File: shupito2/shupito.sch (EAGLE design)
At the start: 89 parts, among them IC2 74LVC1T45, IC3 74LVC1T45, IC4 74LVC1T45, IC5 74LVC1T45, IC6 ATXMEGA32A4U-AU, IC7 TPS73033DBV, Q1 BC807W-1907646, Q10 1758094, Q11 PDTC123YU-1757992, Q2 NX2301P-1894738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

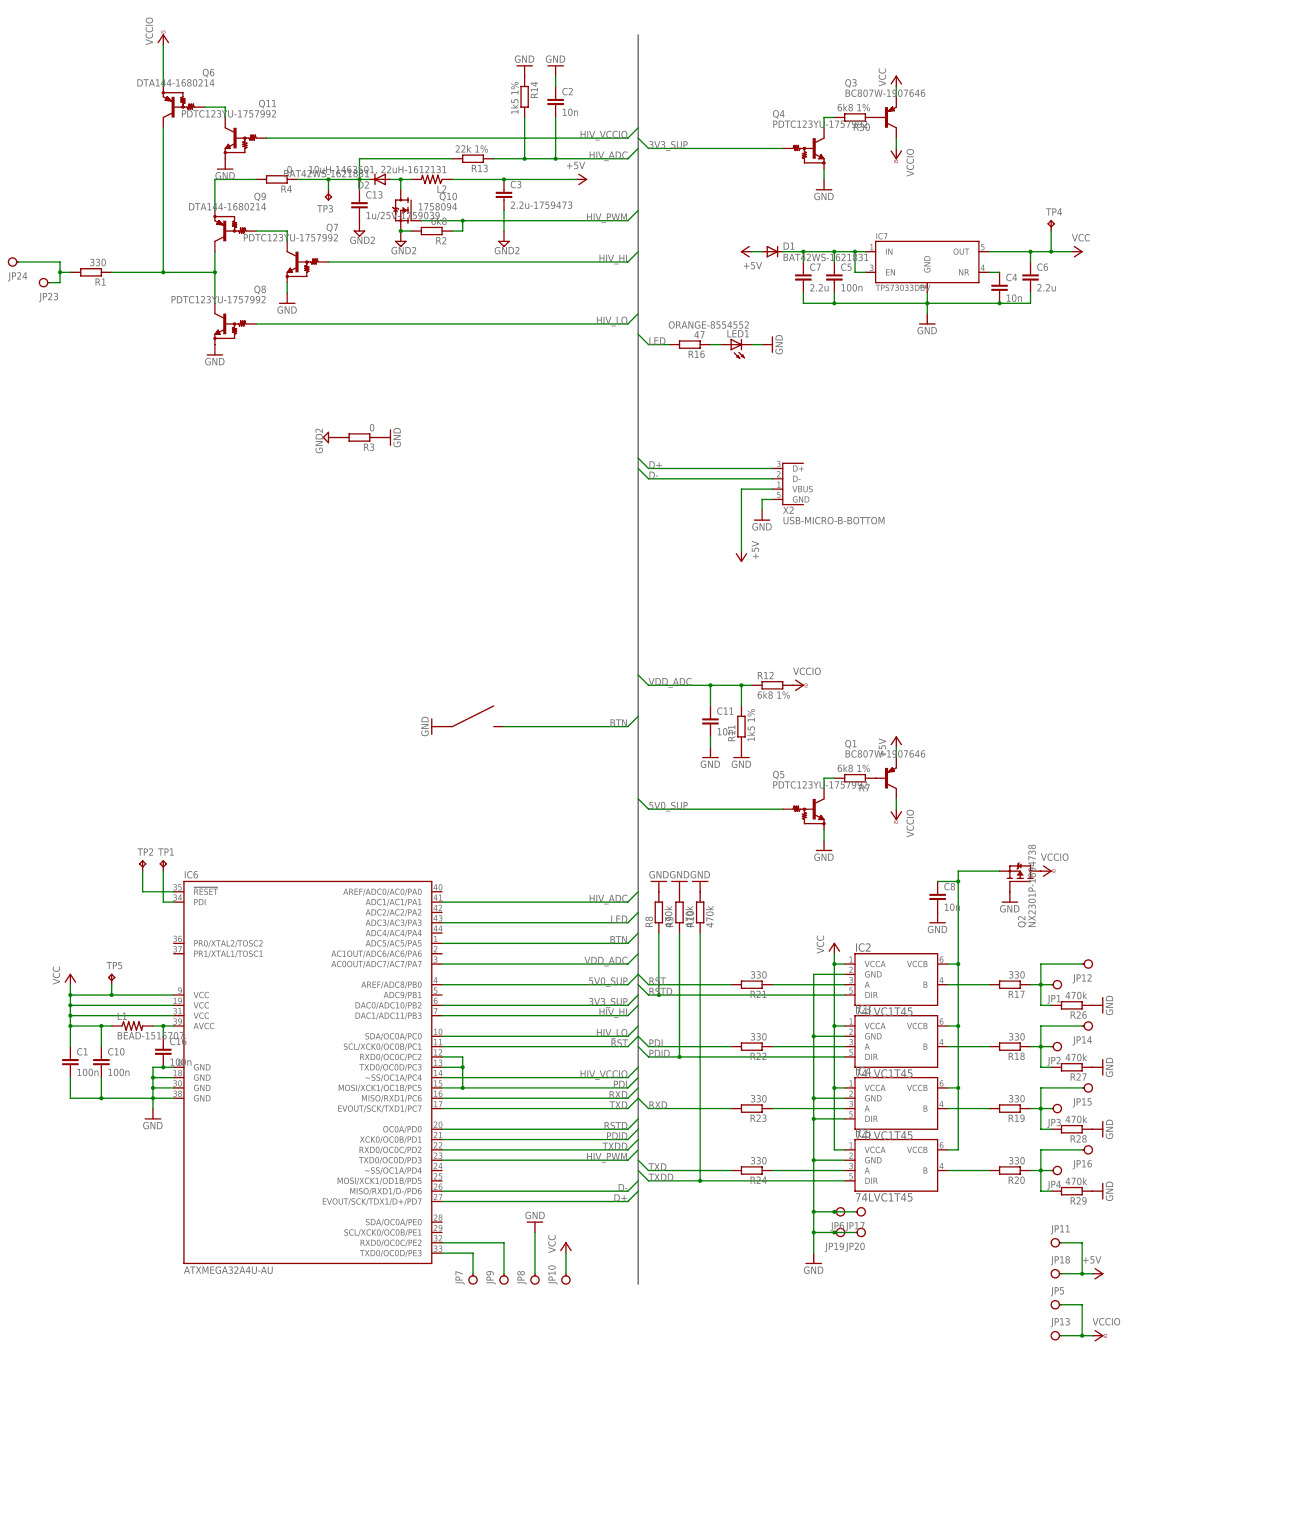
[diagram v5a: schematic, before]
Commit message: Added protective resistors.
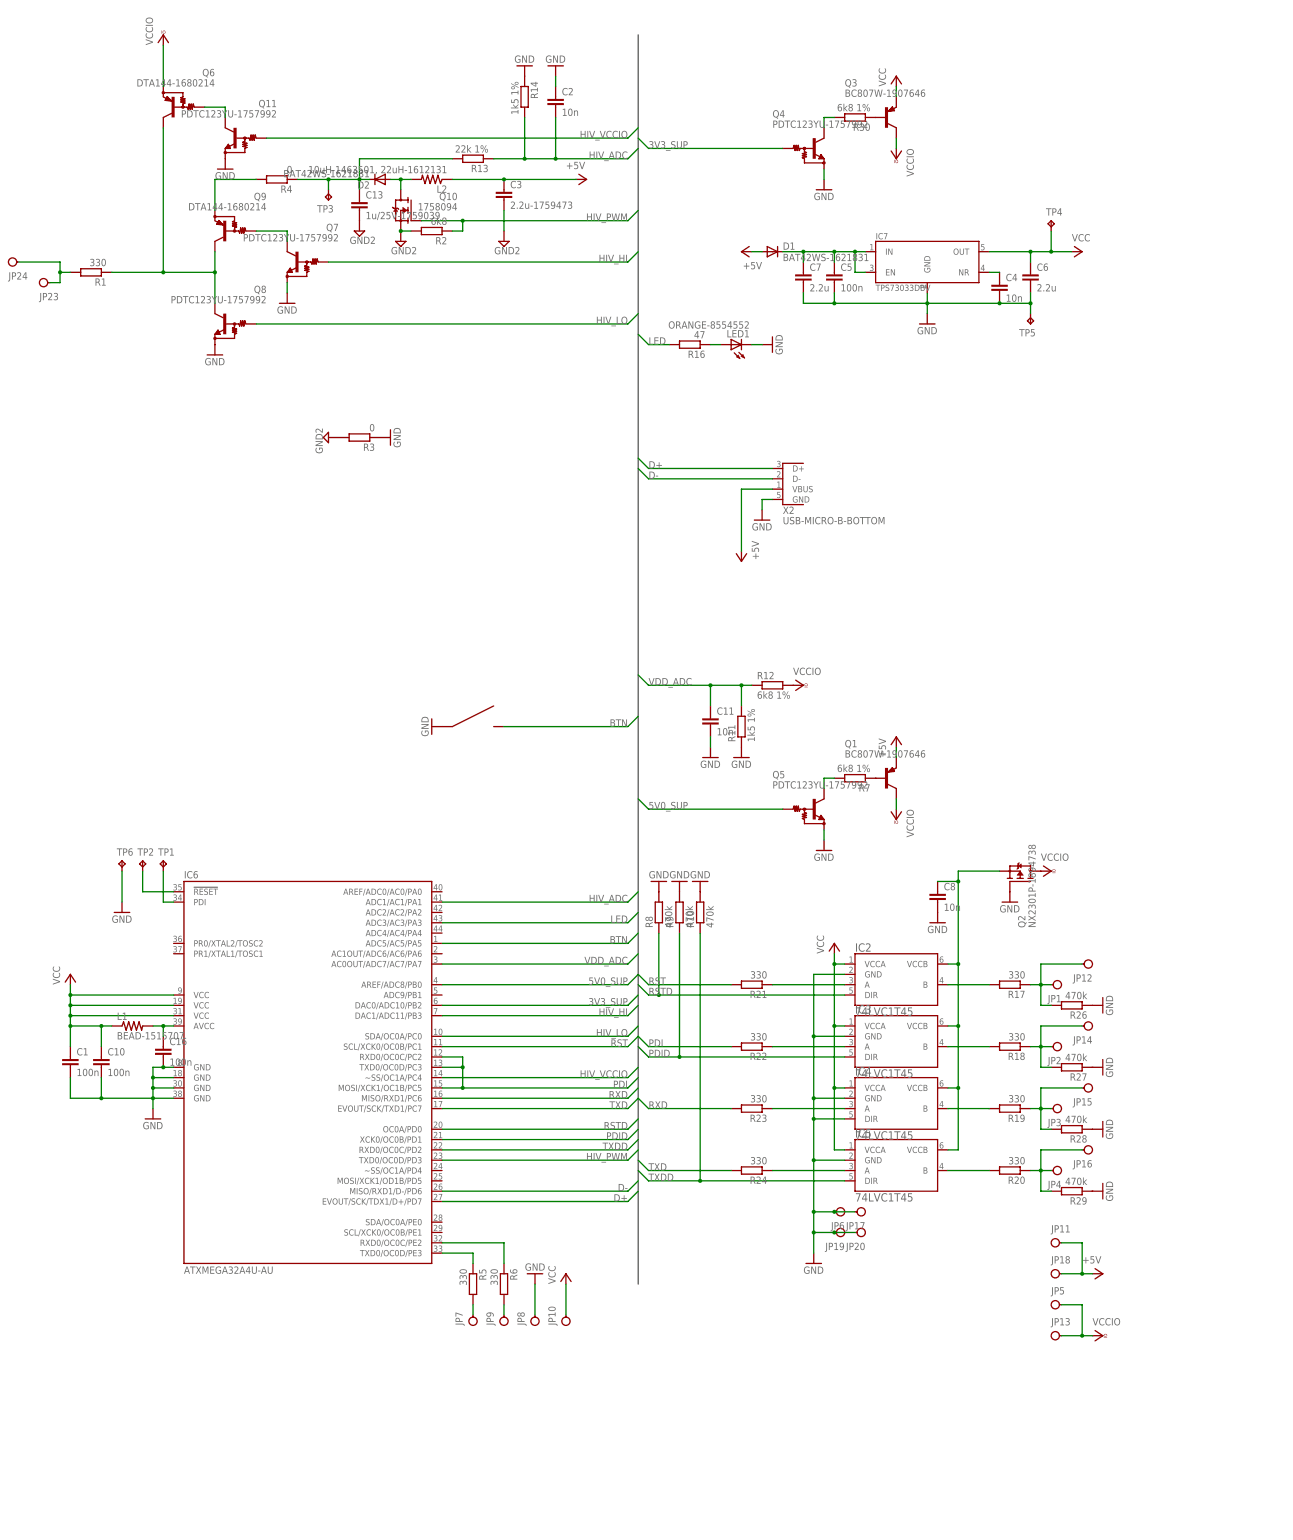
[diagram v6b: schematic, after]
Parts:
- added R5, R6: 330, rcl:R-EU_R0603
- added TP6: TPTP15SQ, testpad:TPTP15SQ
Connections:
- new net N$14: JP7.1, R5.2
- new net N$18: JP9.1, R6.2
- net GND: now also TP5.TP, TP6.TP
- net N$1: now also R5.1; no longer JP7.1
- net N$12: now also R6.1; no longer JP9.1
- net VCC: no longer TP5.TP
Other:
- moved on the sheet: JP10, JP7, JP8, JP9, TP5
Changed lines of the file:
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@@
 </part>
 <part name="R4" library="rcl" deviceset="R-EU_" device="R1206" value="0"/>
+<part name="D1" library="diode" deviceset="DIODE" device="-SOD323" value="BAT42WS-1621831"/>
+<part name="GND15" library="supply1" deviceset="GND" device=""/>
+<part name="P+10" library="supply1" deviceset="VCC" device=""/>
+<part name="TP6" library="testpad" deviceset="TP" device="TP15SQ">
+<attribute name="TP_SIGNAL_NAME" value=""/>
+</part>
+<part name="GND20" library="supply1" deviceset="GND" device=""/>
+<part name="R5" library="rcl" deviceset="R-EU_" device="R0603" value="330"/>
+<part name="R6" library="rcl" deviceset="R-EU_" device="R0603" value="330"/>
 <part name="TP5" library="testpad" deviceset="TP" device="TP15SQ">
 <attribute name="TP_SIGNAL_NAME" value=""/>
 </part>
-<part name="D1" library="diode" deviceset="DIODE" device="-SOD323" value="BAT42WS-1621831"/>
-<part name="GND15" library="supply1" deviceset="GND" device=""/>
-<part name="P+10" library="supply1" deviceset="VCC" device=""/>
 </parts>
 <sheets>
@@
 <instance part="C2" gate="G$1" x="127" y="317.5"/>
 <instance part="GND3" gate="1" x="127" y="325.12" rot="MR180"/>
-<instance part="JP7" gate="G$1" x="106.68" y="25.4" rot="R90"/>
-<instance part="JP8" gate="G$1" x="121.92" y="25.4" rot="R90"/>
-<instance part="JP9" gate="G$1" x="114.3" y="25.4" rot="R90"/>
-<instance part="JP10" gate="G$1" x="129.54" y="25.4" rot="R90"/>
+<instance part="JP7" gate="G$1" x="106.68" y="15.24" rot="R90"/>
+<instance part="JP8" gate="G$1" x="121.92" y="15.24" rot="R90"/>
+<instance part="JP9" gate="G$1" x="114.3" y="15.24" rot="R90"/>
+<instance part="JP10" gate="G$1" x="129.54" y="15.24" rot="R90"/>
 <instance part="C3" gate="G$1" x="114.3" y="294.64"/>
 <instance part="S1" gate="G$1" x="106.68" y="162.56"/>
@@
 <instance part="TP4" gate="G$1" x="248.92" y="287.02"/>
 <instance part="R4" gate="G$1" x="58.42" y="297.18" rot="R180"/>
-<instance part="TP5" gate="G$1" x="17.78" y="101.6"/>
 <instance part="D1" gate="1" x="180.34" y="279.4"/>
-<instance part="GND15" gate="1" x="121.92" y="40.64" rot="R180"/>
-<instance part="P+10" gate="VCC" x="129.54" y="35.56"/>
+<instance part="GND15" gate="1" x="121.92" y="27.94" rot="R180"/>
+<instance part="P+10" gate="VCC" x="129.54" y="27.94"/>
+<instance part="TP6" gate="G$1" x="20.32" y="129.54"/>
+<instance part="GND20" gate="1" x="20.32" y="116.84"/>
+<instance part="R5" gate="G$1" x="106.68" y="25.4" rot="R270"/>
+<instance part="R6" gate="G$1" x="114.3" y="25.4" rot="R270"/>
+<instance part="TP5" gate="G$1" x="243.84" y="261.62" rot="R180"/>
 </instances>
 <busses>
@@
 <wire x1="33.02" y1="93.98" x2="7.62" y2="93.98" width="0.1524" layer="91"/>
 <pinref part="IC6" gate="G$1" pin="VCC@1"/>
-<wire x1="33.02" y1="96.52" x2="17.78" y2="96.52" width="0.1524" layer="91"/>
+<wire x1="33.02" y1="96.52" x2="7.62" y2="96.52" width="0.1524" layer="91"/>
 <junction x="7.62" y="96.52"/>
 <junction x="7.62" y="93.98"/>
 <pinref part="P+4" gate="VCC" pin="VCC"/>
 <pinref part="L1" gate="G$1" pin="1"/>
-<wire x1="17.78" y1="96.52" x2="7.62" y2="96.52" width="0.1524" layer="91"/>
 <wire x1="17.78" y1="88.9" x2="15.24" y2="88.9" width="0.1524" layer="91"/>
 <wire x1="15.24" y1="88.9" x2="7.62" y2="88.9" width="0.1524" layer="91"/>
@@
 <junction x="7.62" y="88.9"/>
 <junction x="15.24" y="88.9"/>
-<pinref part="TP5" gate="G$1" pin="TP"/>
-<wire x1="17.78" y1="99.06" x2="17.78" y2="96.52" width="0.1524" layer="91"/>
-<junction x="17.78" y="96.52"/>
 </segment>
 <segment>
 <pinref part="P+10" gate="VCC" pin="VCC"/>
 <pinref part="JP10" gate="G$1" pin="1"/>
-<wire x1="129.54" y1="33.02" x2="129.54" y2="27.94" width="0.1524" layer="91"/>
+<wire x1="129.54" y1="25.4" x2="129.54" y2="17.78" width="0.1524" layer="91"/>
 </segment>
 </net>
@@
 <pinref part="C7" gate="G$1" pin="2"/>
 <pinref part="C5" gate="G$1" pin="2"/>
+<pinref part="TP5" gate="G$1" pin="TP"/>
+<wire x1="243.84" y1="266.7" x2="243.84" y2="264.16" width="0.1524" layer="91"/>
+<junction x="243.84" y="266.7"/>
 </segment>
 <segment>
@@
 <pinref part="GND15" gate="1" pin="GND"/>
 <pinref part="JP8" gate="G$1" pin="1"/>
-<wire x1="121.92" y1="38.1" x2="121.92" y2="27.94" width="0.1524" layer="91"/>
+<wire x1="121.92" y1="25.4" x2="121.92" y2="17.78" width="0.1524" layer="91"/>
+</segment>
+<segment>
+<pinref part="TP6" gate="G$1" pin="TP"/>
+<pinref part="GND20" gate="1" pin="GND"/>
+<wire x1="20.32" y1="127" x2="20.32" y2="119.38" width="0.1524" layer="91"/>
 </segment>
 </net>
@@
 <segment>
 <pinref part="IC6" gate="G$1" pin="TXD0/OC0D/PE3"/>
-<pinref part="JP7" gate="G$1" pin="1"/>
 <wire x1="99.06" y1="33.02" x2="106.68" y2="33.02" width="0.1524" layer="91"/>
-<wire x1="106.68" y1="33.02" x2="106.68" y2="27.94" width="0.1524" layer="91"/>
+<pinref part="R5" gate="G$1" pin="1"/>
+<wire x1="106.68" y1="33.02" x2="106.68" y2="30.48" width="0.1524" layer="91"/>
 </segment>
 </net>
@@
 <segment>
 <pinref part="IC6" gate="G$1" pin="RXD0/OC0C/PE2"/>
-<pinref part="JP9" gate="G$1" pin="1"/>
 <wire x1="99.06" y1="35.56" x2="114.3" y2="35.56" width="0.1524" layer="91"/>
-<wire x1="114.3" y1="35.56" x2="114.3" y2="27.94" width="0.1524" layer="91"/>
+<pinref part="R6" gate="G$1" pin="1"/>
+<wire x1="114.3" y1="35.56" x2="114.3" y2="30.48" width="0.1524" layer="91"/>
 </segment>
 </net>
@@
 </segment>
 </net>
+<net name="N$14" class="0">
+<segment>
+<pinref part="JP7" gate="G$1" pin="1"/>
+<pinref part="R5" gate="G$1" pin="2"/>
+<wire x1="106.68" y1="17.78" x2="106.68" y2="20.32" width="0.1524" layer="91"/>
+</segment>
+</net>
+<net name="N$18" class="0">
+<segment>
+<pinref part="JP9" gate="G$1" pin="1"/>
+<pinref part="R6" gate="G$1" pin="2"/>
+<wire x1="114.3" y1="17.78" x2="114.3" y2="20.32" width="0.1524" layer="91"/>
+</segment>
+</net>

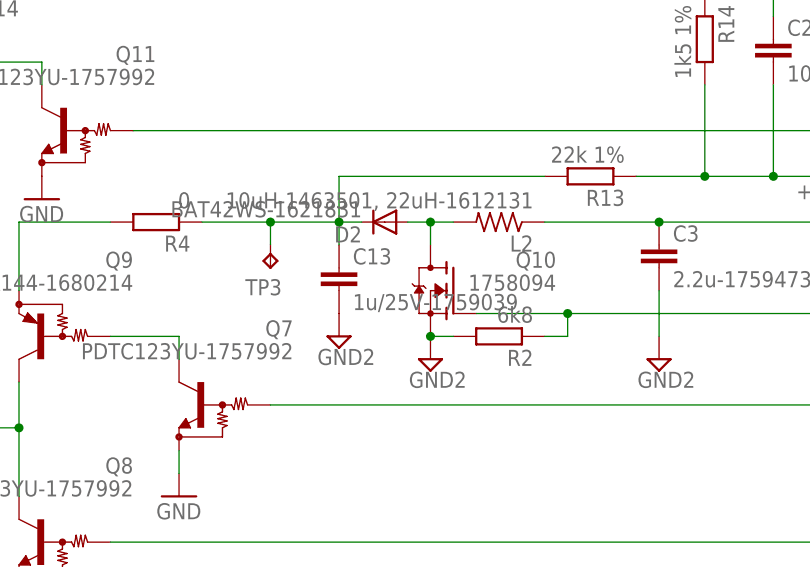
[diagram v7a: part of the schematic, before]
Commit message: Added a part name.
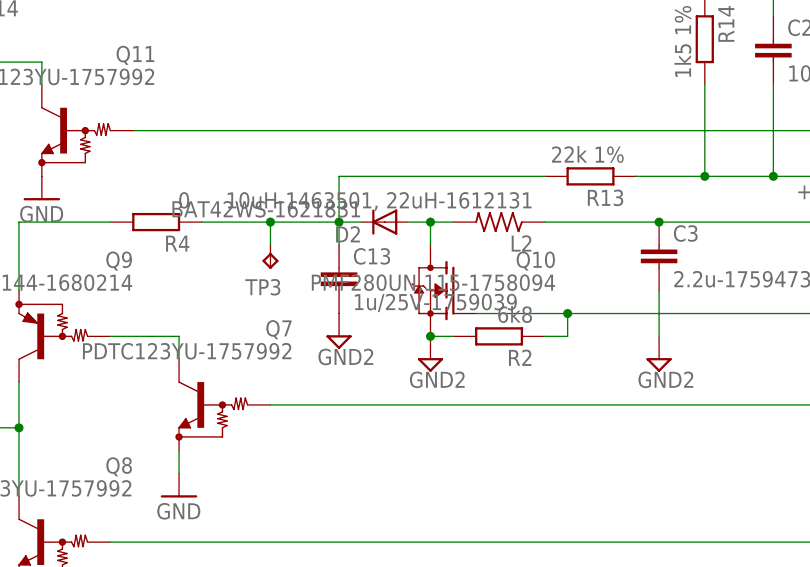
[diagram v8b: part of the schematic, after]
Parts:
- Q10: value 1758094 -> PMF280UN,115-1758094
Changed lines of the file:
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@@
 <part name="C13" library="rcl" deviceset="C-EU" device="C0603K" value="1u/25V-1759039"/>
 <part name="D2" library="diode" deviceset="DIODE" device="-SOD323" value="BAT42WS-1621831"/>
-<part name="Q10" library="transistors" deviceset="N-MOSFET" device="-SOT323-GSD" value="1758094"/>
+<part name="Q10" library="transistors" deviceset="N-MOSFET" device="-SOT323-GSD" value="PMF280UN,115-1758094"/>
 <part name="R1" library="rcl" deviceset="R-EU_" device="R0603" value="330"/>
 <part name="R2" library="rcl" deviceset="R-EU_" device="R0603" value="6k8"/>
